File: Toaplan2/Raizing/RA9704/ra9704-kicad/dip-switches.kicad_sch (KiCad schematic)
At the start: 9 parts, among them SW1 SW_DIP_x08, SW2 SW_DIP_x08, SW3 SW_DIP_x08, U325 74HC240, U326 74HC240, U332 74HC240

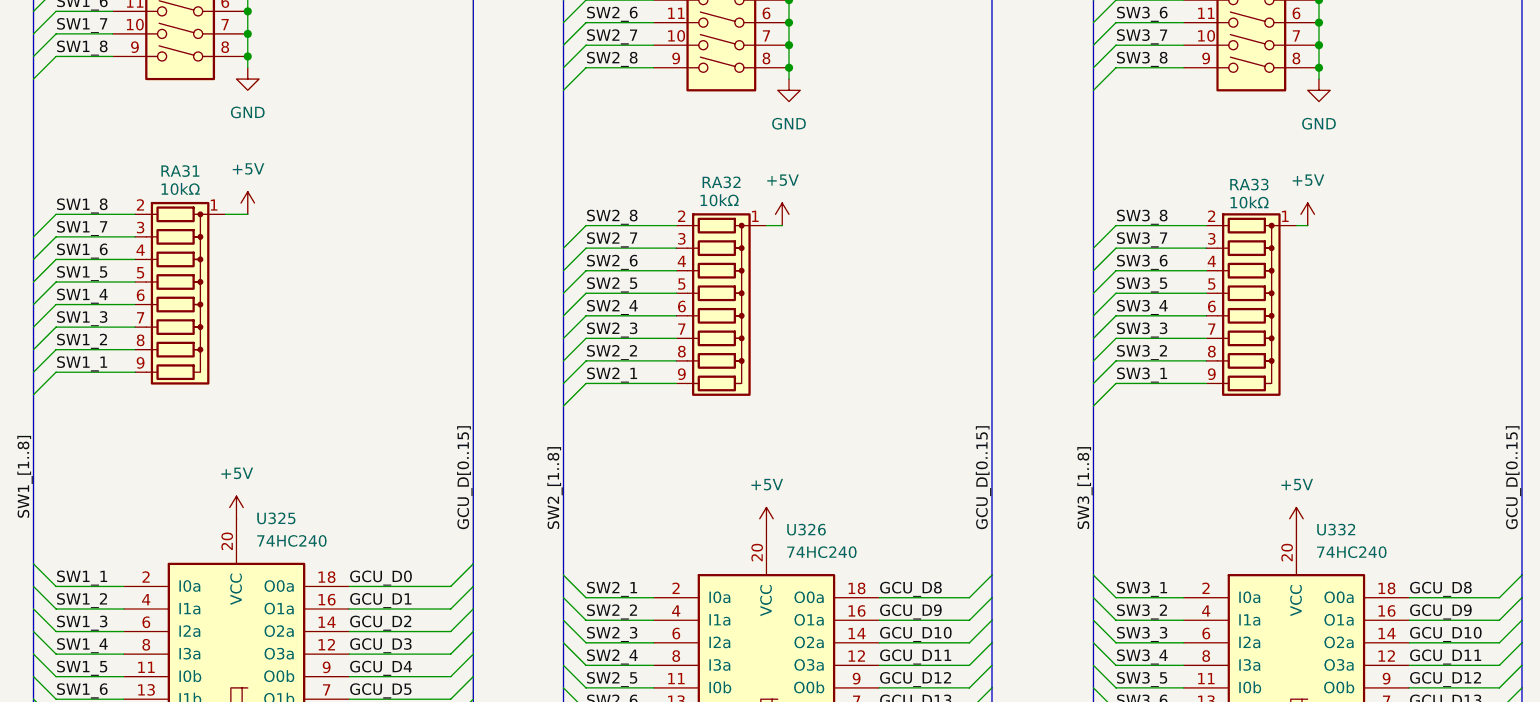
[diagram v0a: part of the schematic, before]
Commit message: fix(ra9704): Add Os as a proxy for 0s in all reference designators
RA9704 has reference designators such that each number has a preceding zero (e.g. RA076, U074, etc.). This causes a bug in KiCAD.

This is 'fixed' by using the 'O' (the letter 'Oh') character instead.

For more info, see the following issue on the KiCAD Gitlab repo

https://gitlab.com/kicad/code/kicad/-/issues/19229
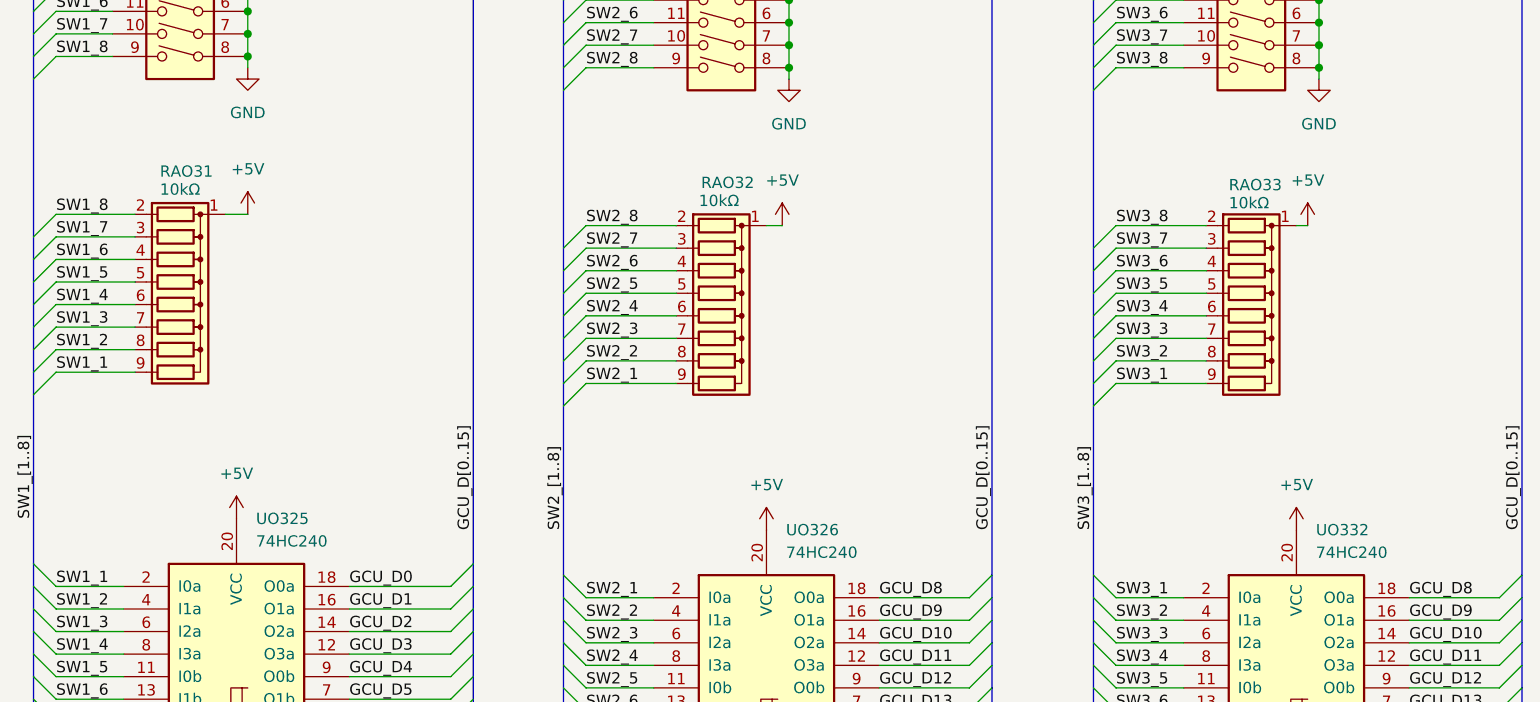
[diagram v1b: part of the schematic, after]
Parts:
- renumbered RA31 to RAO31, RA32 to RAO32, RA33 to RAO33, U325 to UO325, U326 to UO326, U332 to UO332
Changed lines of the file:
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@@
 		(on_board yes)
 		(dnp no)
-		(property "Reference" "RA33"
+		(property "Reference" "RAO33"
 			(at 165.1 95.758 90)
 			(effects
@@
 			(project "ra9704"
 				(path "/24d3b4cf-2360-45fc-8c40-cedc8afdf9e1/8f77968a-d5b7-4368-9f67-422488c409cc"
-					(reference "RA33")
+					(reference "RAO33")
 					(unit 1)
 				)
@@
 		(dnp no)
 		(fields_autoplaced yes)
-		(property "Reference" "U326"
+		(property "Reference" "UO326"
 			(at 115.2241 134.62 0)
 			(effects
@@
 			(project "ra9704"
 				(path "/24d3b4cf-2360-45fc-8c40-cedc8afdf9e1/8f77968a-d5b7-4368-9f67-422488c409cc"
-					(reference "U326")
+					(reference "UO326")
 					(unit 1)
 				)
@@
 		(dnp no)
 		(fields_autoplaced yes)
-		(property "Reference" "U325"
+		(property "Reference" "UO325"
 			(at 55.5341 133.35 0)
 			(effects
@@
 			(project "ra9704"
 				(path "/24d3b4cf-2360-45fc-8c40-cedc8afdf9e1/8f77968a-d5b7-4368-9f67-422488c409cc"
-					(reference "U325")
+					(reference "UO325")
 					(unit 1)
 				)
@@
 		(dnp no)
 		(fields_autoplaced yes)
-		(property "Reference" "U332"
+		(property "Reference" "UO332"
 			(at 174.9141 134.62 0)
 			(effects
@@
 			(project "ra9704"
 				(path "/24d3b4cf-2360-45fc-8c40-cedc8afdf9e1/8f77968a-d5b7-4368-9f67-422488c409cc"
-					(reference "U332")
+					(reference "UO332")
 					(unit 1)
 				)
@@
 		(on_board yes)
 		(dnp no)
-		(property "Reference" "RA32"
+		(property "Reference" "RAO32"
 			(at 105.664 95.504 90)
 			(effects
@@
 			(project "ra9704"
 				(path "/24d3b4cf-2360-45fc-8c40-cedc8afdf9e1/8f77968a-d5b7-4368-9f67-422488c409cc"
-					(reference "RA32")
+					(reference "RAO32")
 					(unit 1)
 				)
@@
 		(on_board yes)
 		(dnp no)
-		(property "Reference" "RA31"
+		(property "Reference" "RAO31"
 			(at 44.704 94.234 90)
 			(effects
@@
 			(project "ra9704"
 				(path "/24d3b4cf-2360-45fc-8c40-cedc8afdf9e1/8f77968a-d5b7-4368-9f67-422488c409cc"
-					(reference "RA31")
-					(unit 1)
-				)
+					(reference "RAO31")
+					(unit 1)
+				)
